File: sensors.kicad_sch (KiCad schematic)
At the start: 14 parts, among them J4 Hirose U.FL, U3 ICM-42688-P, U4 NEO-M8M

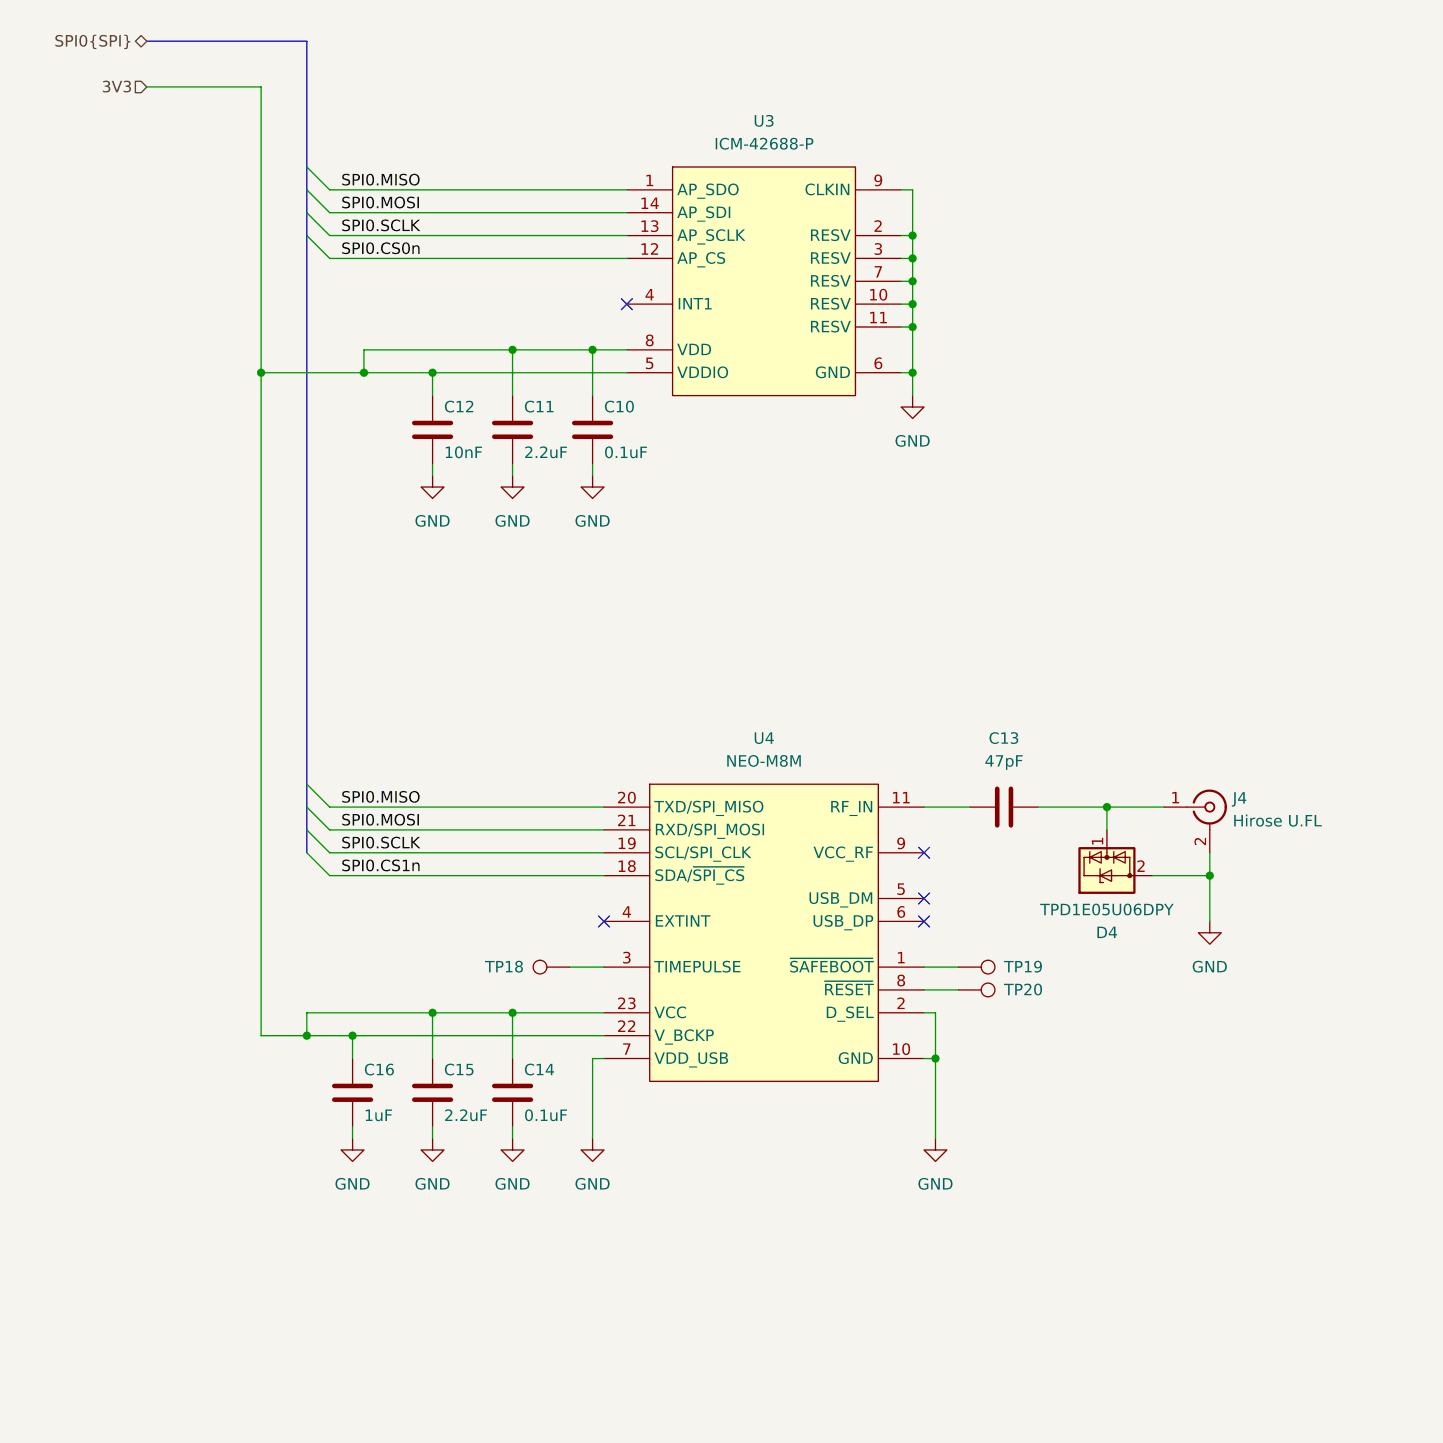
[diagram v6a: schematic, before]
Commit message: un-abstraction, footprints, layout edge cuts
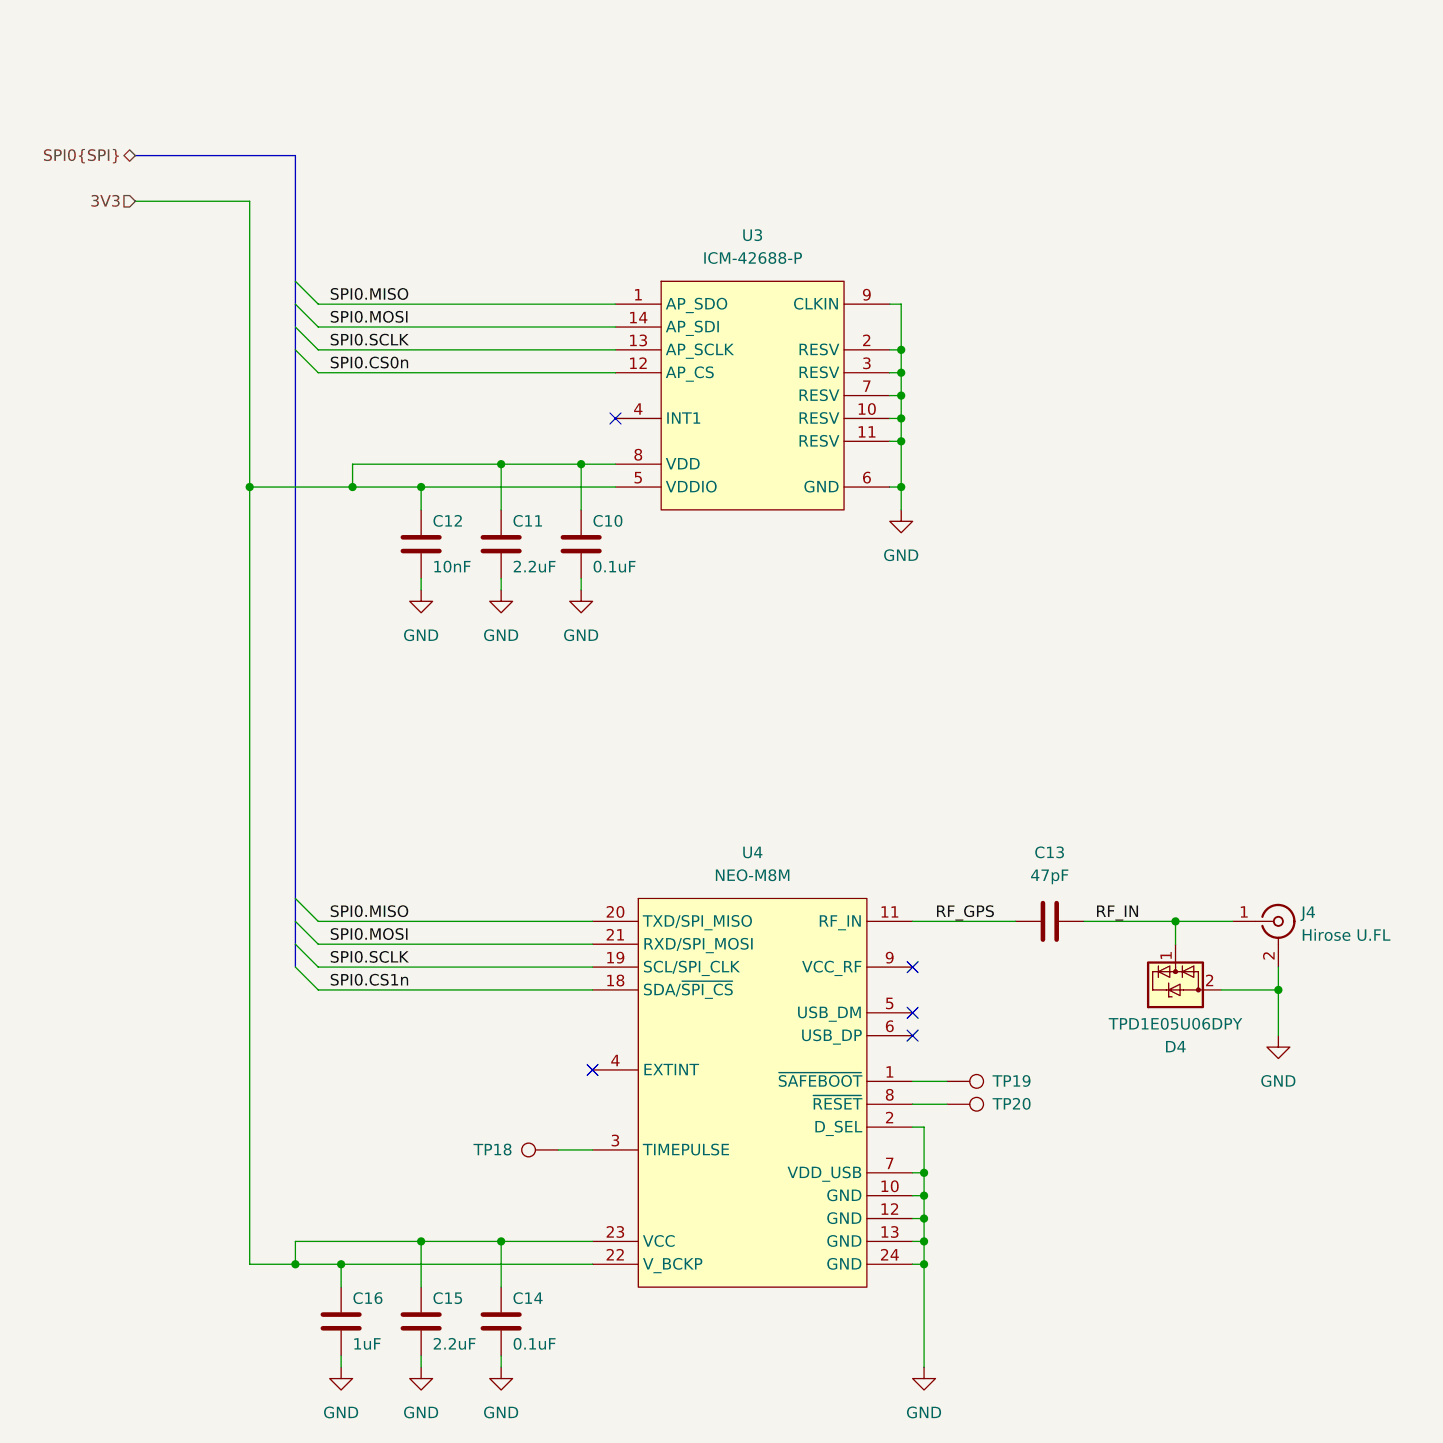
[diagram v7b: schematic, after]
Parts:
- C13: footprint (none) -> Capacitor_SMD:C_0402_1005Metric
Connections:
- net GND: now also U4.12 (GND), U4.13 (GND), U4.24 (GND); no longer U4.14 (RESERVED)
- net RF_IN: now reaches C13.2, D4.1 (I/O), J4.1 (In)
- net RF_GPS: now reaches C13.1, U4.11 (RF_IN)
- now unconnected: U4.15 (RESERVED), U4.16 (RESERVED), U4.17 (RESERVED)
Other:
- moved on the sheet: C10, C11, C12, C13, C14, C15, C16, D4, J4, TP18, TP19, TP20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

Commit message: moved power TPs to cm5 sheet
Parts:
- C13: symbol Device:C -> library:C
- D4: symbol Power_Protection:TPD1E05U06DPY -> library:TPD1E05U06DPY
- J4: symbol Connector:Conn_Coaxial -> library:Conn_Coaxial
- TP18, TP19, TP20: symbol Connector:TestPoint -> library:TestPoint
- U4: symbol RF_GPS:NEO-M8M -> library:NEO-M8M
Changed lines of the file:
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@@
 	)
 	(symbol
-		(lib_id "Connector:TestPoint")
+		(lib_id "library:TestPoint")
 		(at 127 138.43 270)
 		(unit 1)
@@
 	)
 	(symbol
-		(lib_id "Power_Protection:TPD1E05U06DPY")
+		(lib_id "library:TPD1E05U06DPY")
 		(at 152.4 125.73 0)
 		(mirror x)
@@
 	)
 	(symbol
-		(lib_id "Device:C")
+		(lib_id "library:C")
 		(at 138.43 118.11 90)
 		(unit 1)
@@
 	)
 	(symbol
-		(lib_id "Connector:TestPoint")
+		(lib_id "library:TestPoint")
 		(at 127 135.89 270)
 		(unit 1)
@@
 	)
 	(symbol
-		(lib_id "Connector:Conn_Coaxial")
+		(lib_id "library:Conn_Coaxial")
 		(at 163.83 118.11 0)
 		(unit 1)
@@
 	)
 	(symbol
-		(lib_id "RF_GPS:NEO-M8M")
+		(lib_id "library:NEO-M8M")
 		(at 105.41 132.08 0)
 		(unit 1)
@@
 	)
 	(symbol
-		(lib_id "Connector:TestPoint")
+		(lib_id "library:TestPoint")
 		(at 83.82 143.51 90)
 		(unit 1)
